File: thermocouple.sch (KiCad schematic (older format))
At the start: 10 parts, among them J4 1935161, Q4 Q_PMOS_GSD, U2 MAX31856

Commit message: Add pcb, update packages
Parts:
- C2, C3, C4, C5, C6: footprint Capacitors_SMD:C_0603 -> Capacitor_SMD:C_0603_1608Metric
- D4: footprint Diodes_SMD:D_0603 -> Diode_SMD:D_0603_1608Metric
- Q4: footprint TO_SOT_Packages_SMD:SOT-23 -> Package_TO_SOT_SMD:SOT-23
- R7: footprint Resistors_SMD:R_0603 -> Resistor_SMD:R_0603_1608Metric
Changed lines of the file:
@@
 AR Path="/5B8ADEE2/5B8B5D8B" Ref="U?"  Part="1"
 AR Path="/5B8DE3E9/5B8B5D8B" Ref="U3"  Part="1"
-F 0 "U2" H 5800 4728 50  0000 C CNN
+F 0 "U3" H 5800 4728 50  0000 C CNN
 F 1 "MAX31856" H 5800 4637 50  0000 C CNN
 F 2 "Package_SO:TSSOP-14_4.4x5mm_P0.65mm" H 5950 3400 50  0001 L CNN
@@
 AR Path="/5B8ADEE2/5B8B8EAA" Ref="C?"  Part="1"
 AR Path="/5B8DE3E9/5B8B8EAA" Ref="C10"  Part="1"
-F 0 "C5" H 5515 3296 50  0000 L CNN
+F 0 "C10" H 5515 3296 50  0000 L CNN
 F 1 "0.1uF" H 5515 3205 50  0000 L CNN
-F 2 "Capacitors_SMD:C_0603" H 5438 3100 50  0001 C CNN
+F 2 "Capacitor_SMD:C_0603_1608Metric" H 5438 3100 50  0001 C CNN
 F 3 "http://www.samsungsem.com/kr/support/product-search/mlcc/CL10F104ZO8NNNC.jsp" H 5400 3250 50  0001 C CNN
 F 4 "1276-1258-1-ND" H 5400 3250 50  0001 C CNN "DigikeyPartNumber"
@@
 AR Path="/5B8ADEE2/5B8B8EBE" Ref="C?"  Part="1"
 AR Path="/5B8DE3E9/5B8B8EBE" Ref="C8"  Part="1"
-F 0 "C3" H 4815 4046 50  0000 L CNN
+F 0 "C8" H 4815 4046 50  0000 L CNN
 F 1 "0.1uF" H 4815 3955 50  0000 L CNN
-F 2 "Capacitors_SMD:C_0603" H 4738 3850 50  0001 C CNN
+F 2 "Capacitor_SMD:C_0603_1608Metric" H 4738 3850 50  0001 C CNN
 F 3 "http://www.samsungsem.com/kr/support/product-search/mlcc/CL10F104ZO8NNNC.jsp" H 4700 4000 50  0001 C CNN
 F 4 "1276-1258-1-ND" H 4700 4000 50  0001 C CNN "DigikeyPartNumber"
@@
 AR Path="/5B8ADEE2/5B8B9109" Ref="J?"  Part="1"
 AR Path="/5B8DE3E9/5B8B9109" Ref="J5"  Part="1"
-F 0 "J4" H 4230 3996 50  0000 L CNN
+F 0 "J5" H 4230 3996 50  0000 L CNN
 F 1 "1935161" H 4230 3905 50  0000 L CNN
 F 2 "1935161:PHOENIX_1935161" H 4100 3950 50  0001 L BNN
@@
 AR Path="/5B8ADEE2/5B8C85E4" Ref="C?"  Part="1"
 AR Path="/5B8DE3E9/5B8C85E4" Ref="C11"  Part="1"
-F 0 "C6" H 6315 3296 50  0000 L CNN
+F 0 "C11" H 6315 3296 50  0000 L CNN
 F 1 "0.1uF" H 6315 3205 50  0000 L CNN
-F 2 "Capacitors_SMD:C_0603" H 6238 3100 50  0001 C CNN
+F 2 "Capacitor_SMD:C_0603_1608Metric" H 6238 3100 50  0001 C CNN
 F 3 "http://www.samsungsem.com/kr/support/product-search/mlcc/CL10F104ZO8NNNC.jsp" H 6200 3250 50  0001 C CNN
 F 4 "1276-1258-1-ND" H 6200 3250 50  0001 C CNN "DigikeyPartNumber"
@@
 AR Path="/5B8ADEE2/5B8C908D" Ref="C?"  Part="1"
 AR Path="/5B8DE3E9/5B8C908D" Ref="C9"  Part="1"
-F 0 "C4" H 4815 4346 50  0000 L CNN
+F 0 "C9" H 4815 4346 50  0000 L CNN
 F 1 "0.01uF" H 4815 4255 50  0000 L CNN
-F 2 "Capacitors_SMD:C_0603" H 4738 4150 50  0001 C CNN
+F 2 "Capacitor_SMD:C_0603_1608Metric" H 4738 4150 50  0001 C CNN
 F 3 "http://datasheets.avx.com/X7RDielectric.pdf" H 4700 4300 50  0001 C CNN
 F 4 "478-1227-1-ND" H 4700 4300 50  0001 C CNN "DigikeyPartNumber"
@@
 AR Path="/5B8ADEE2/5B8C91FE" Ref="C?"  Part="1"
 AR Path="/5B8DE3E9/5B8C91FE" Ref="C7"  Part="1"
-F 0 "C2" H 4815 3746 50  0000 L CNN
+F 0 "C7" H 4815 3746 50  0000 L CNN
 F 1 "0.01uF" H 4815 3655 50  0000 L CNN
-F 2 "Capacitors_SMD:C_0603" H 4738 3550 50  0001 C CNN
+F 2 "Capacitor_SMD:C_0603_1608Metric" H 4738 3550 50  0001 C CNN
 F 3 "http://datasheets.avx.com/X7RDielectric.pdf" H 4700 3700 50  0001 C CNN
 F 4 "478-1227-1-ND" H 4700 3700 50  0001 C CNN "DigikeyPartNumber"
@@
 AR Path="/5B8ADEE2/5B8C9DFB" Ref="Q?"  Part="1"
 AR Path="/5B8DE3E9/5B8C9DFB" Ref="Q5"  Part="1"
-F 0 "Q4" H 7306 3796 50  0000 L CNN
+F 0 "Q5" H 7306 3796 50  0000 L CNN
 F 1 "Q_PMOS_GSD" H 7306 3705 50  0000 L CNN
-F 2 "TO_SOT_Packages_SMD:SOT-23" H 7300 3850 50  0001 C CNN
+F 2 "Package_TO_SOT_SMD:SOT-23" H 7300 3850 50  0001 C CNN
 F 3 "http://www.onsemi.com/pub/Collateral/NTR5105P-D.PDF" H 7100 3750 50  0001 C CNN
 F 4 "NTR5105PT1GOSCT-ND" H 7100 3750 50  0001 C CNN "DigikeyPartNumber"
@@
 AR Path="/5B8ADEE2/5B8CA624" Ref="D?"  Part="1"
 AR Path="/5B8DE3E9/5B8CA624" Ref="D5"  Part="1"
-F 0 "D4" H 7492 3895 50  0000 C CNN
+F 0 "D5" H 7492 3895 50  0000 C CNN
 F 1 "RED" H 7492 3986 50  0000 C CNN
-F 2 "Diodes_SMD:D_0603" H 7500 4150 50  0001 C CNN
+F 2 "Diode_SMD:D_0603_1608Metric" H 7500 4150 50  0001 C CNN
 F 3 "https://katalog.we-online.de/led/datasheet/150060RS75000.pdf" H 7500 4150 50  0001 C CNN
 F 4 "732-4978-1-ND" H 7500 4150 50  0001 C CNN "DigikeyPartNumber"
@@
 AR Path="/5B8ADEE2/5B8CA62C" Ref="R?"  Part="1"
 AR Path="/5B8DE3E9/5B8CA62C" Ref="R8"  Part="1"
-F 0 "R7" V 8057 4150 50  0000 C CNN
+F 0 "R8" V 8057 4150 50  0000 C CNN
 F 1 "470" V 7966 4150 50  0000 C CNN
-F 2 "Resistors_SMD:R_0603" V 7780 4150 50  0001 C CNN
+F 2 "Resistor_SMD:R_0603_1608Metric" V 7780 4150 50  0001 C CNN
 F 3 "https://industrial.panasonic.com/cdbs/www-data/pdf/RDA0000/AOA0000C304.pdf" H 7850 4150 50  0001 C CNN
 F 4 "P470HCT-ND" H 7850 4150 50  0001 C CNN "DigikeyPartNumber"

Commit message: Add a bunch of stuff
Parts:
- removed J4: 1935161, 1935161:PHOENIX_1935161, symbol 1935161:1935161
- removed Q4: Q_PMOS_GSD, Package_TO_SOT_SMD:SOT-23, symbol Device:Q_PMOS_GSD
- added Q3: Q_PNP_BEC, Package_TO_SOT_SMD:SC-59, symbol Device:Q_PNP_BEC
- added R6: 100, Resistor_SMD:R_0603_1608Metric, symbol Device:R
- added R8: 47k, Resistor_SMD:R_0603_1608Metric, symbol Device:R
- C2, C4: DigikeyPartNumber 478-1227-1-ND -> 1276-1921-1-ND
- R7: value 470 -> 100; DigikeyPartNumber P470HCT-ND -> P100HCT-ND
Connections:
- net labels added: T+, T-
- wire segments 36 -> 34
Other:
- moved on the sheet: D5
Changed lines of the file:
@@
 	1    0    0    -1
 $EndComp
-$Comp
-L 1935161:1935161 J?
-U 1 1 5B8B9109
-P 4100 3950
-AR Path="/5B8B9109" Ref="J?"  Part="1"
-AR Path="/5B8AB544/5B8B9109" Ref="J4"  Part="1"
-AR Path="/5B8ADEE2/5B8B9109" Ref="J?"  Part="1"
-AR Path="/5B8DE3E9/5B8B9109" Ref="J5"  Part="1"
-F 0 "J5" H 4230 3996 50  0000 L CNN
-F 1 "1935161" H 4230 3905 50  0000 L CNN
-F 2 "1935161:PHOENIX_1935161" H 4100 3950 50  0001 L BNN
-F 3 "Phoenix Contact" H 4100 3950 50  0001 L BNN
-F 4 "None" H 4100 3950 50  0001 L BNN "Field4"
-F 5 "Conn Terminal Blocks 2 POS 5mm Solder ST Thru-Hole 16A" H 4100 3950 50  0001 L BNN "Field5"
-F 6 "None" H 4100 3950 50  0001 L BNN "Field6"
-F 7 "1935161" H 4100 3950 50  0001 L BNN "Field7"
-F 8 "Unavailable" H 4100 3950 50  0001 L BNN "Field8"
-F 9 "277-1667-ND" H 4100 3950 50  0001 C CNN "DigikeyPartNumber"
-	1    4100 3950
-	-1   0    0    1
-$EndComp
-Wire Wire Line
-	4400 4050 4500 4050
-Wire Wire Line
-	4500 4050 4500 4150
-Wire Wire Line
-	4500 4150 4700 4150
 Wire Wire Line
 	4700 4150 5050 4150
@@
 Connection ~ 5800 4600
 $Comp
-L Device:C C4
-U 1 1 5B8C908D
-P 4700 4300
-AR Path="/5B8AB544/5B8C908D" Ref="C4"  Part="1"
-AR Path="/5B8ADEE2/5B8C908D" Ref="C?"  Part="1"
-AR Path="/5B8DE3E9/5B8C908D" Ref="C9"  Part="1"
-F 0 "C9" H 4815 4346 50  0000 L CNN
-F 1 "0.01uF" H 4815 4255 50  0000 L CNN
-F 2 "Capacitor_SMD:C_0603_1608Metric" H 4738 4150 50  0001 C CNN
-F 3 "http://datasheets.avx.com/X7RDielectric.pdf" H 4700 4300 50  0001 C CNN
-F 4 "478-1227-1-ND" H 4700 4300 50  0001 C CNN "DigikeyPartNumber"
-	1    4700 4300
-	1    0    0    -1
-$EndComp
-$Comp
 L power:GND #PWR0110
 U 1 1 5B8C91A5
@@
 F 1 "0.01uF" H 4815 3655 50  0000 L CNN
 F 2 "Capacitor_SMD:C_0603_1608Metric" H 4738 3550 50  0001 C CNN
-F 3 "http://datasheets.avx.com/X7RDielectric.pdf" H 4700 3700 50  0001 C CNN
-F 4 "478-1227-1-ND" H 4700 3700 50  0001 C CNN "DigikeyPartNumber"
+F 3 "http://www.samsungsem.com/kr/support/product-search/mlcc/__icsFiles/afieldfile/2018/07/24/CL10B103KB8NCNC.pdf" H 4700 3700 50  0001 C CNN
+F 4 "1276-1921-1-ND" H 4700 3700 50  0001 C CNN "DigikeyPartNumber"
 	1    4700 3700
 	1    0    0    -1
@@
 $EndComp
 $Comp
-L Device:Q_PMOS_GSD Q?
-U 1 1 5B8C9DFB
-P 7100 3750
-AR Path="/5B8C9DFB" Ref="Q?"  Part="1"
-AR Path="/5B8AB544/5B8C9DFB" Ref="Q4"  Part="1"
-AR Path="/5B8ADEE2/5B8C9DFB" Ref="Q?"  Part="1"
-AR Path="/5B8DE3E9/5B8C9DFB" Ref="Q5"  Part="1"
-F 0 "Q5" H 7306 3796 50  0000 L CNN
-F 1 "Q_PMOS_GSD" H 7306 3705 50  0000 L CNN
-F 2 "Package_TO_SOT_SMD:SOT-23" H 7300 3850 50  0001 C CNN
-F 3 "http://www.onsemi.com/pub/Collateral/NTR5105P-D.PDF" H 7100 3750 50  0001 C CNN
-F 4 "NTR5105PT1GOSCT-ND" H 7100 3750 50  0001 C CNN "DigikeyPartNumber"
-	1    7100 3750
-	1    0    0    -1
-$EndComp
-$Comp
 L power:+3V3 #PWR0112
 U 1 1 5B8CA2E0
-P 7200 3550
+P 7600 3650
 AR Path="/5B8AB544/5B8CA2E0" Ref="#PWR0112"  Part="1"
 AR Path="/5B8ADEE2/5B8CA2E0" Ref="#PWR0121"  Part="1"
 AR Path="/5B8DE3E9/5B8CA2E0" Ref="#PWR0121"  Part="1"
-F 0 "#PWR0121" H 7200 3400 50  0001 C CNN
-F 1 "+3V3" H 7215 3723 50  0000 C CNN
-F 2 "" H 7200 3550 50  0001 C CNN
-F 3 "" H 7200 3550 50  0001 C CNN
-	1    7200 3550
+F 0 "#PWR0121" H 7600 3500 50  0001 C CNN
+F 1 "+3V3" H 7615 3823 50  0000 C CNN
+F 2 "" H 7600 3650 50  0001 C CNN
+F 3 "" H 7600 3650 50  0001 C CNN
+	1    7600 3650
 	1    0    0    -1
 $EndComp
@@
 L Device:LED D?
 U 1 1 5B8CA624
-P 7500 4150
+P 7900 4250
 AR Path="/5B8CA624" Ref="D?"  Part="1"
 AR Path="/5B8AB544/5B8CA624" Ref="D4"  Part="1"
 AR Path="/5B8ADEE2/5B8CA624" Ref="D?"  Part="1"
 AR Path="/5B8DE3E9/5B8CA624" Ref="D5"  Part="1"
-F 0 "D5" H 7492 3895 50  0000 C CNN
-F 1 "RED" H 7492 3986 50  0000 C CNN
-F 2 "Diode_SMD:D_0603_1608Metric" H 7500 4150 50  0001 C CNN
-F 3 "https://katalog.we-online.de/led/datasheet/150060RS75000.pdf" H 7500 4150 50  0001 C CNN
-F 4 "732-4978-1-ND" H 7500 4150 50  0001 C CNN "DigikeyPartNumber"
-	1    7500 4150
+F 0 "D5" H 7892 3995 50  0000 C CNN
+F 1 "RED" H 7892 4086 50  0000 C CNN
+F 2 "Diode_SMD:D_0603_1608Metric" H 7900 4250 50  0001 C CNN
+F 3 "https://katalog.we-online.de/led/datasheet/150060RS75000.pdf" H 7900 4250 50  0001 C CNN
+F 4 "732-4978-1-ND" H 7900 4250 50  0001 C CNN "DigikeyPartNumber"
+	1    7900 4250
 	-1   0    0    1
 $EndComp
-$Comp
-L Device:R R?
-U 1 1 5B8CA62C
-P 7850 4150
-AR Path="/5B8CA62C" Ref="R?"  Part="1"
-AR Path="/5B8AB544/5B8CA62C" Ref="R7"  Part="1"
-AR Path="/5B8ADEE2/5B8CA62C" Ref="R?"  Part="1"
-AR Path="/5B8DE3E9/5B8CA62C" Ref="R8"  Part="1"
-F 0 "R8" V 8057 4150 50  0000 C CNN
-F 1 "470" V 7966 4150 50  0000 C CNN
-F 2 "Resistor_SMD:R_0603_1608Metric" V 7780 4150 50  0001 C CNN
-F 3 "https://industrial.panasonic.com/cdbs/www-data/pdf/RDA0000/AOA0000C304.pdf" H 7850 4150 50  0001 C CNN
-F 4 "P470HCT-ND" H 7850 4150 50  0001 C CNN "DigikeyPartNumber"
-	1    7850 4150
-	0    1    1    0
-$EndComp
-Wire Wire Line
-	7650 4150 7700 4150
-Wire Wire Line
-	8000 4150 8050 4150
-Wire Wire Line
-	7350 4150 7200 4150
+Wire Wire Line
+	8050 4250 8100 4250
+Wire Wire Line
+	7750 4250 7600 4250
 $Comp
 L power:GND #PWR?
 U 1 1 5B8CA636
-P 8050 4100
+P 8100 4250
 AR Path="/5B8CA636" Ref="#PWR?"  Part="1"
 AR Path="/5B8AB544/5B8CA636" Ref="#PWR0113"  Part="1"
 AR Path="/5B8ADEE2/5B8CA636" Ref="#PWR0122"  Part="1"
 AR Path="/5B8DE3E9/5B8CA636" Ref="#PWR0122"  Part="1"
-F 0 "#PWR0122" H 8050 3850 50  0001 C CNN
-F 1 "GND" H 8055 3927 50  0000 C CNN
-F 2 "" H 8050 4100 50  0001 C CNN
-F 3 "" H 8050 4100 50  0001 C CNN
-	1    8050 4100
-	-1   0    0    1
-$EndComp
-Wire Wire Line
-	8050 4150 8050 4100
-Wire Wire Line
-	7200 3950 7200 4150
+F 0 "#PWR0122" H 8100 4000 50  0001 C CNN
+F 1 "GND" H 8105 4077 50  0000 C CNN
+F 2 "" H 8100 4250 50  0001 C CNN
+F 3 "" H 8100 4250 50  0001 C CNN
+	1    8100 4250
+	0    -1   -1   0
+$EndComp
+Wire Wire Line
+	7600 4050 7600 4250
 Text HLabel 6600 3650 2    50   Input ~ 0
 DRDY
@@
 Text HLabel 6600 3750 2    50   Input ~ 0
 FAULT
-Wire Wire Line
-	6300 3750 6550 3750
-Wire Wire Line
-	6550 3750 6550 3800
-Wire Wire Line
-	6550 3800 6900 3800
-Wire Wire Line
-	6900 3800 6900 3750
-Connection ~ 6550 3750
-Wire Wire Line
-	6550 3750 6600 3750
 Text HLabel 6600 3950 2    50   Input ~ 0
 CS
@@
 Wire Wire Line
 	6300 4250 6600 4250
+$Comp
+L Device:R R6
+U 1 1 5BAD7E31
+P 4250 3850
+AR Path="/5B8AB544/5BAD7E31" Ref="R6"  Part="1"
+AR Path="/5B8DE3E9/5BAD7E31" Ref="R9"  Part="1"
+F 0 "R9" V 4043 3850 50  0000 C CNN
+F 1 "100" V 4134 3850 50  0000 C CNN
+F 2 "Resistor_SMD:R_0603_1608Metric" V 4180 3850 50  0001 C CNN
+F 3 "https://industrial.panasonic.com/cdbs/www-data/pdf/RDA0000/AOA0000C304.pdf" H 4250 3850 50  0001 C CNN
+F 4 "P100HCT-ND" H 4250 3850 50  0001 C CNN "DigikeyPartNumber"
+	1    4250 3850
+	0    1    1    0
+$EndComp
+Wire Wire Line
+	4400 4150 4700 4150
+Wire Wire Line
+	3950 3850 4100 3850
+$Comp
+L Device:R R7
+U 1 1 5BADB677
+P 4250 4150
+AR Path="/5B8AB544/5BADB677" Ref="R7"  Part="1"
+AR Path="/5B8DE3E9/5BADB677" Ref="R10"  Part="1"
+F 0 "R10" V 4043 4150 50  0000 C CNN
+F 1 "100" V 4134 4150 50  0000 C CNN
+F 2 "Resistor_SMD:R_0603_1608Metric" V 4180 4150 50  0001 C CNN
+F 3 "https://industrial.panasonic.com/cdbs/www-data/pdf/RDA0000/AOA0000C304.pdf" H 4250 4150 50  0001 C CNN
+F 4 "P100HCT-ND" H 4250 4150 50  0001 C CNN "DigikeyPartNumber"
+	1    4250 4150
+	0    1    1    0
+$EndComp
+Wire Wire Line
+	6300 3750 6450 3750
+$Comp
+L Device:Q_PNP_BEC Q3
+U 1 1 5BADF07C
+P 7500 3850
+AR Path="/5B8AB544/5BADF07C" Ref="Q3"  Part="1"
+AR Path="/5B8DE3E9/5BADF07C" Ref="Q4"  Part="1"
+F 0 "Q4" H 7691 3896 50  0000 L CNN
+F 1 "Q_PNP_BEC" H 7691 3805 50  0000 L CNN
+F 2 "Package_TO_SOT_SMD:SC-59" H 7700 3950 50  0001 C CNN
+F 3 "https://media.digikey.com/pdf/Data%20Sheets/Diodes%20PDFs/MMBT3906.pdf" H 7500 3850 50  0001 C CNN
+F 4 "MMBT3906-FDICT-ND" H 7500 3850 50  0001 C CNN "DigikeyPartNumber"
+	1    7500 3850
+	1    0    0    -1
+$EndComp
+$Comp
+L Device:R R8
+U 1 1 5BAE219E
+P 7100 3850
+AR Path="/5B8AB544/5BAE219E" Ref="R8"  Part="1"
+AR Path="/5B8DE3E9/5BAE219E" Ref="R11"  Part="1"
+F 0 "R11" V 6893 3850 50  0000 C CNN
+F 1 "47k" V 6984 3850 50  0000 C CNN
+F 2 "Resistor_SMD:R_0603_1608Metric" V 7030 3850 50  0001 C CNN
+F 3 "https://industrial.panasonic.com/cdbs/www-data/pdf/RDA0000/AOA0000C304.pdf" H 7100 3850 50  0001 C CNN
+F 4 "P47.0KHCT-ND" H 7100 3850 50  0001 C CNN "DigikeyPartNumber"
+	1    7100 3850
+	0    1    1    0
+$EndComp
+Wire Wire Line
+	7250 3850 7300 3850
+Wire Wire Line
+	6950 3850 6450 3850
+Wire Wire Line
+	6450 3850 6450 3750
+Connection ~ 6450 3750
+Wire Wire Line
+	6450 3750 6600 3750
+Text HLabel 3950 3850 0    50   Input ~ 0
+T+
+Text HLabel 3950 4150 0    50   Input ~ 0
+T-
+Wire Wire Line
+	3950 4150 4100 4150
+$Comp
+L Device:C C4
+U 1 1 5BB11D31
+P 4700 4300
+AR Path="/5B8AB544/5BB11D31" Ref="C4"  Part="1"
+AR Path="/5B8ADEE2/5BB11D31" Ref="C?"  Part="1"
+AR Path="/5B8DE3E9/5BB11D31" Ref="C9"  Part="1"
+F 0 "C9" H 4815 4346 50  0000 L CNN
+F 1 "0.01uF" H 4815 4255 50  0000 L CNN
+F 2 "Capacitor_SMD:C_0603_1608Metric" H 4738 4150 50  0001 C CNN
+F 3 "http://www.samsungsem.com/kr/support/product-search/mlcc/__icsFiles/afieldfile/2018/07/24/CL10B103KB8NCNC.pdf" H 4700 4300 50  0001 C CNN
+F 4 "1276-1921-1-ND" H 4700 4300 50  0001 C CNN "DigikeyPartNumber"
+	1    4700 4300
+	1    0    0    -1
+$EndComp
 $EndSCHEMATC

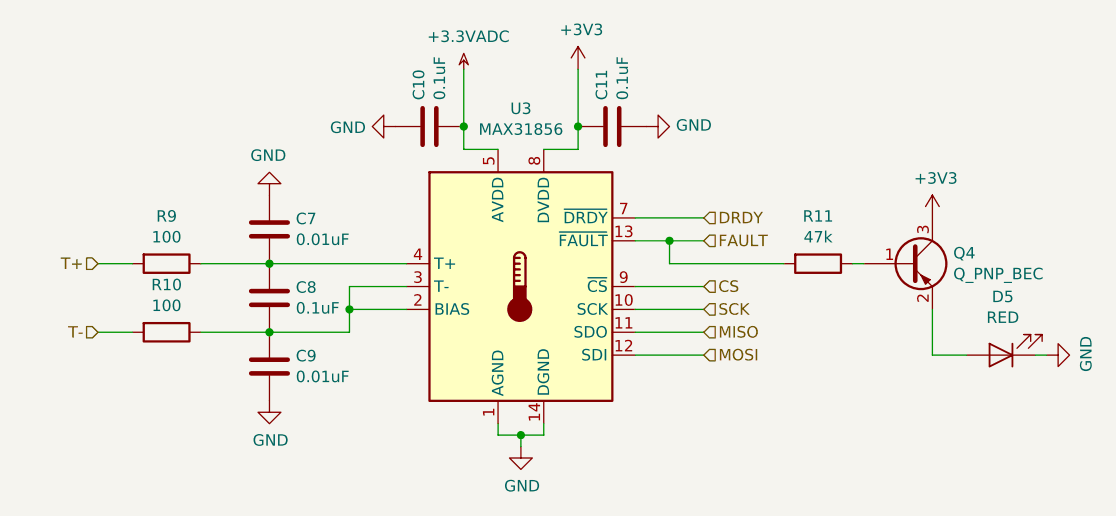
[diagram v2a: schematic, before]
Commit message: UPdate transistor wiring
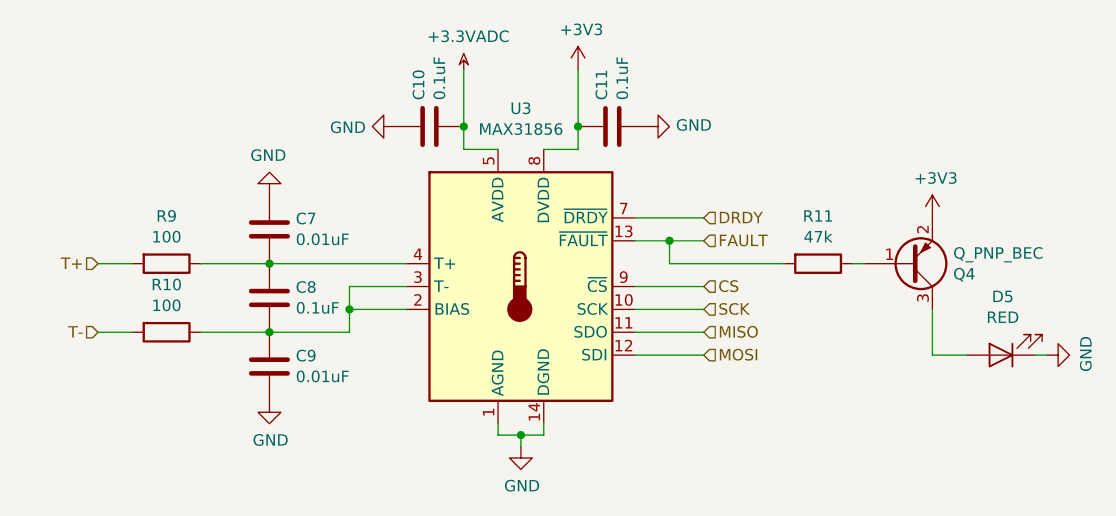
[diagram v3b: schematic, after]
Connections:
- net +3V3: now also Q3.2 (E); no longer Q3.3 (C)
- net at D4.2 (A): now also Q3.3 (C); no longer Q3.2 (E)
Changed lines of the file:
@@
 $Descr A4 11693 8268
 encoding utf-8
-Sheet 2 3
+Sheet 3 3
 Title ""
 Date ""
@@
 	6300 3750 6450 3750
 $Comp
-L Device:Q_PNP_BEC Q3
-U 1 1 5BADF07C
-P 7500 3850
-AR Path="/5B8AB544/5BADF07C" Ref="Q3"  Part="1"
-AR Path="/5B8DE3E9/5BADF07C" Ref="Q4"  Part="1"
-F 0 "Q4" H 7691 3896 50  0000 L CNN
-F 1 "Q_PNP_BEC" H 7691 3805 50  0000 L CNN
-F 2 "Package_TO_SOT_SMD:SC-59" H 7700 3950 50  0001 C CNN
-F 3 "https://media.digikey.com/pdf/Data%20Sheets/Diodes%20PDFs/MMBT3906.pdf" H 7500 3850 50  0001 C CNN
-F 4 "MMBT3906-FDICT-ND" H 7500 3850 50  0001 C CNN "DigikeyPartNumber"
-	1    7500 3850
-	1    0    0    -1
-$EndComp
-$Comp
 L Device:R R8
 U 1 1 5BAE219E
@@
 	1    0    0    -1
 $EndComp
+$Comp
+L Device:Q_PNP_BEC Q3
+U 1 1 5BADF07C
+P 7500 3850
+AR Path="/5B8AB544/5BADF07C" Ref="Q3"  Part="1"
+AR Path="/5B8DE3E9/5BADF07C" Ref="Q4"  Part="1"
+F 0 "Q4" H 7691 3896 50  0000 L CNN
+F 1 "Q_PNP_BEC" H 7691 3805 50  0000 L CNN
+F 2 "Package_TO_SOT_SMD:SC-59" H 7700 3950 50  0001 C CNN
+F 3 "https://media.digikey.com/pdf/Data%20Sheets/Diodes%20PDFs/MMBT3906.pdf" H 7500 3850 50  0001 C CNN
+F 4 "MMBT3906-FDICT-ND" H 7500 3850 50  0001 C CNN "DigikeyPartNumber"
+	1    7500 3850
+	1    0    0    1
+$EndComp
 $EndSCHEMATC
